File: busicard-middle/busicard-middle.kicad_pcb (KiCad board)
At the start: 2 copper layers, 70 x 46 mm, 8 parts

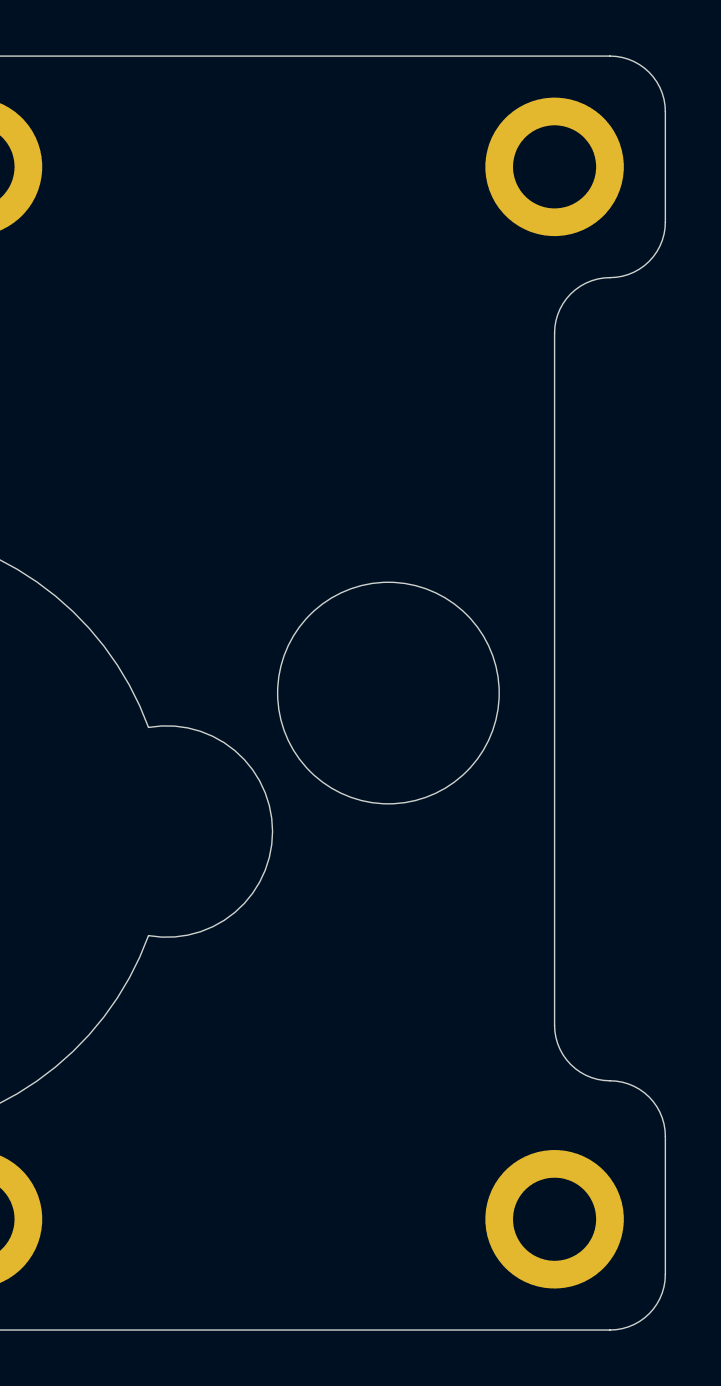
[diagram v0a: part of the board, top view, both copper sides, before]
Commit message: First pass at ready for production
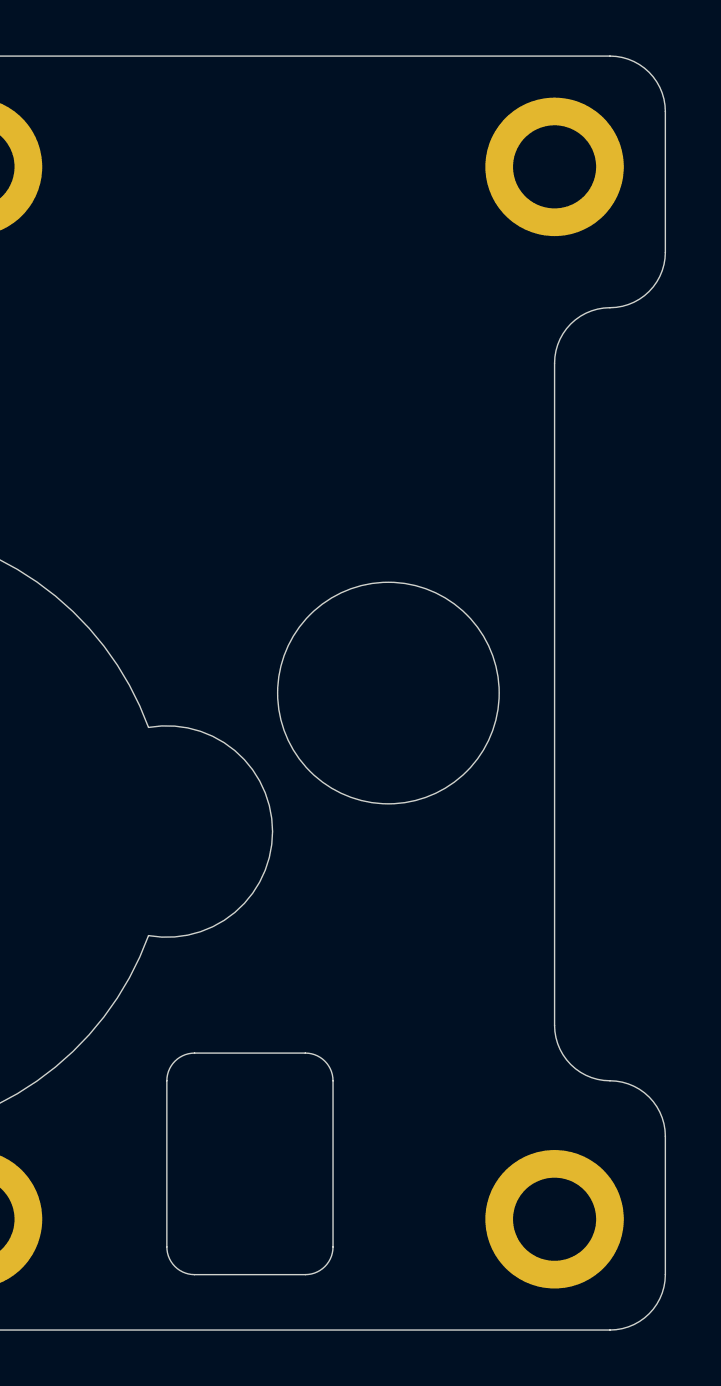
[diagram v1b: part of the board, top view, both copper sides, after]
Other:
- outline, holes or cut-outs redrawn
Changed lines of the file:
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@@
+	)
+	(gr_rect
+		(start 182 113)
+		(end 188 121)
+		(stroke
+			(width 0.1)
+			(type dot)
+		)
+		(fill none)
+		(layer "Dwgs.User")
 	)
 	(gr_rect
@@
 		(layer "Edge.Cuts")
 	)
+	(gr_line
+		(start 183 121)
+		(end 187 121)
+		(stroke
+			(width 0.05)
+			(type default)
+		)
+		(layer "Edge.Cuts")
+	)
 	(gr_arc
 		(start 155.337728 91.240826)
@@
 	)
 	(gr_arc
-		(start 196 87)
-		(mid 196.585786 85.585786)
-		(end 198 85)
+		(start 188 120)
+		(mid 187.707107 120.707107)
+		(end 187 121)
+		(stroke
+			(width 0.05)
+			(type default)
+		)
+		(layer "Edge.Cuts")
+	)
+	(gr_line
+		(start 188 120)
+		(end 188 114)
+		(stroke
+			(width 0.05)
+			(type default)
+		)
+		(layer "Edge.Cuts")
+	)
+	(gr_arc
+		(start 196 88.085786)
+		(mid 196.585786 86.671572)
+		(end 198 86.085786)
+		(stroke
+			(width 0.05)
+			(type default)
+		)
+		(layer "Edge.Cuts")
+	)
+	(gr_arc
+		(start 182 114)
+		(mid 182.292893 113.292893)
+		(end 183 113)
 		(stroke
 			(width 0.05)
@@
 		(layer "Edge.Cuts")
 	)
+	(gr_line
+		(start 183 113)
+		(end 187 113)
+		(stroke
+			(width 0.05)
+			(type default)
+		)
+		(layer "Edge.Cuts")
+	)
 	(gr_arc
 		(start 198 114)
@@
 		(layer "Edge.Cuts")
 	)
-	(gr_line
-		(start 196 87)
-		(end 196 112)
+	(gr_arc
+		(start 187 113)
+		(mid 187.707107 113.292893)
+		(end 188 114)
 		(stroke
 			(width 0.05)
@@
 	)
 	(gr_line
+		(start 200 84.085786)
+		(end 200 79)
+		(stroke
+			(width 0.05)
+			(type default)
+		)
+		(layer "Edge.Cuts")
+	)
+	(gr_line
 		(start 130 121)
 		(end 130 79)
@@
 	)
 	(gr_line
-		(start 200 79)
-		(end 200 83)
+		(start 196 88.085786)
+		(end 196 112)
 		(stroke
 			(width 0.05)
@@
 	)
 	(gr_arc
-		(start 200 83)
-		(mid 199.414214 84.414214)
-		(end 198 85)
+		(start 200 84.085786)
+		(mid 199.414214 85.5)
+		(end 198 86.085786)
+		(stroke
+			(width 0.05)
+			(type default)
+		)
+		(layer "Edge.Cuts")
+	)
+	(gr_line
+		(start 182 120)
+		(end 182 114)
 		(stroke
 			(width 0.05)
@@
 		(stroke
 			(width 0.05)
+			(type default)
+		)
+		(layer "Edge.Cuts")
+	)
+	(gr_arc
+		(start 183 121)
+		(mid 182.292893 120.707107)
+		(end 182 120)
+		(stroke
+			(width 0.05)

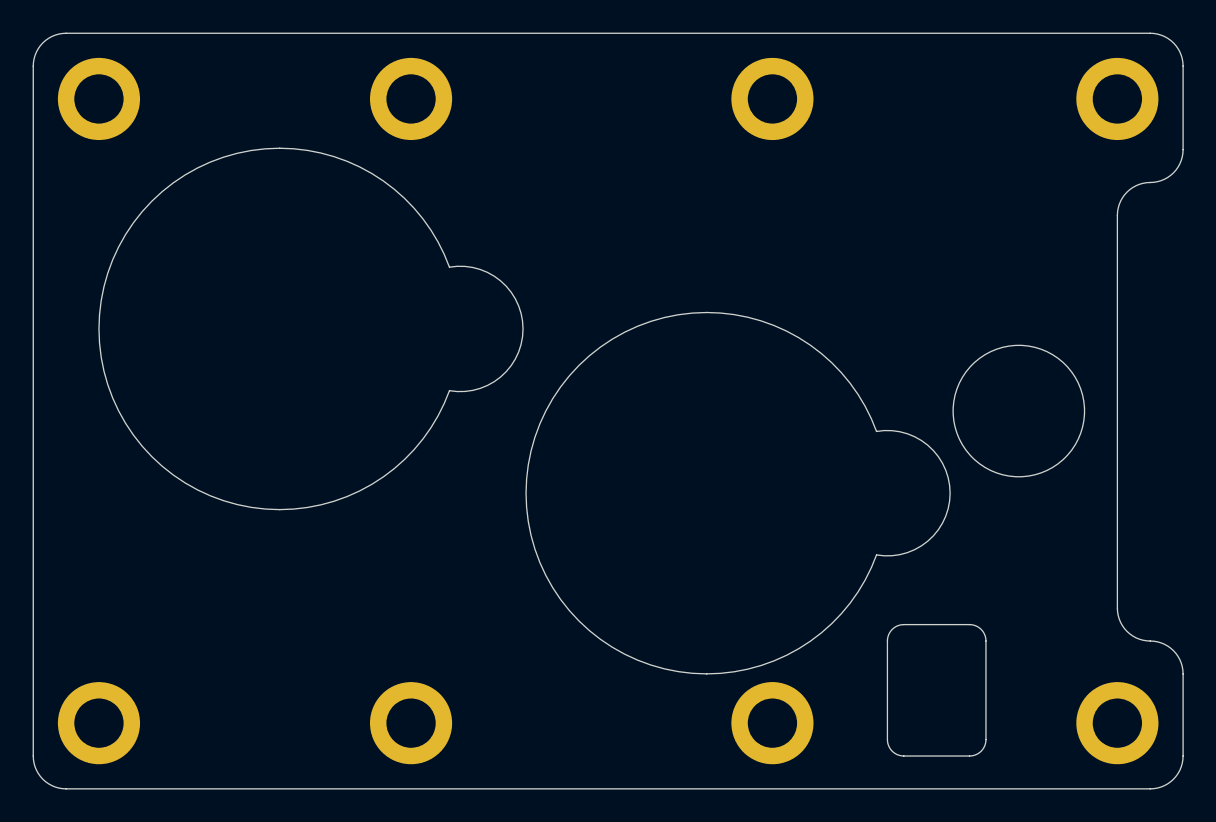
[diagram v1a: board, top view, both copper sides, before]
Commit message: More steps to production
- add slik
- add paste to battery pads
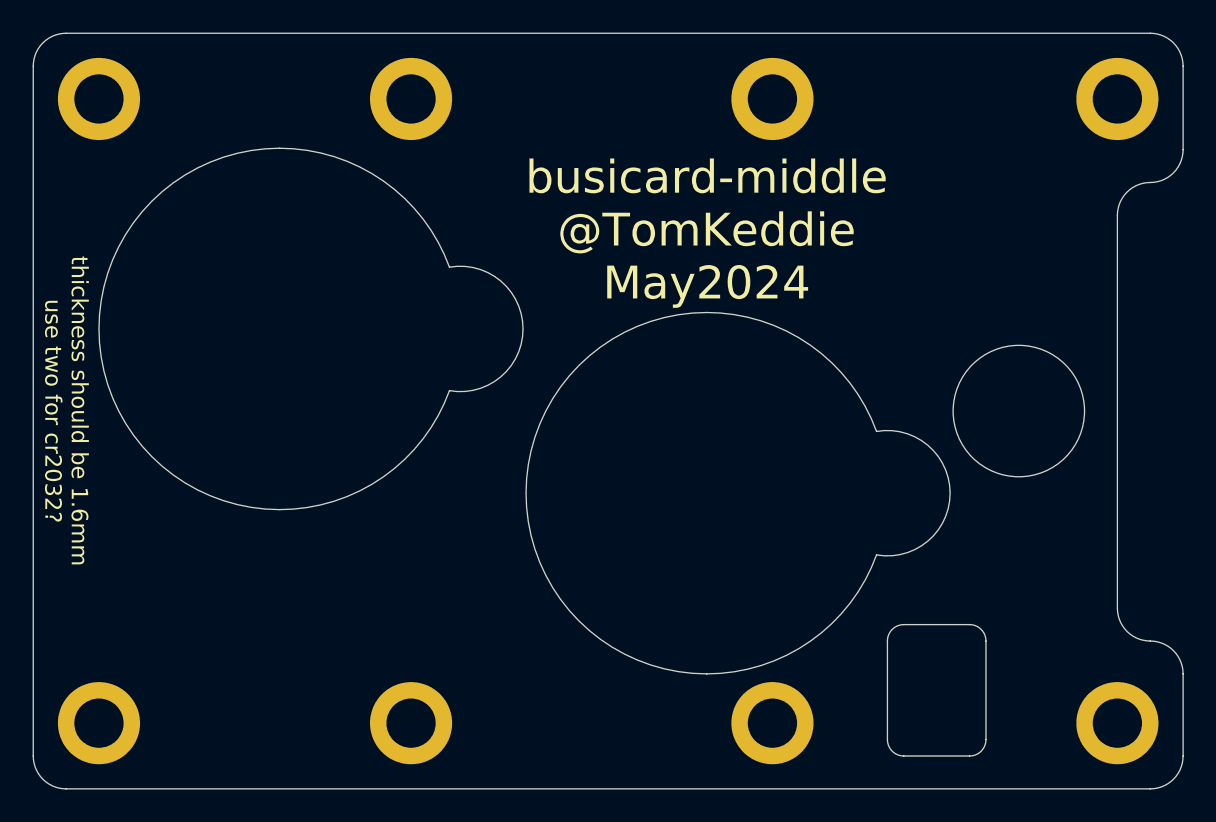
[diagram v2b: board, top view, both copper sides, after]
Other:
- board text added: "busicard-middle @TomKeddie May2024"
- board text added: "thickness should be 1.6mm use two for cr2032?"
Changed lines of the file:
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@@
 		(layer "Edge.Cuts")
 	)
+	(gr_text "thickness should be 1.6mm\nuse two for cr2032?"
+		(at 132 100 270)
+		(layer "F.SilkS")
+		(effects
+			(font
+				(size 1 1)
+				(thickness 0.1)
+			)
+		)
+	)
+	(gr_text "busicard-middle\n@TomKeddie\nMay2024"
+		(at 171 89 0)
+		(layer "F.SilkS")
+		(effects
+			(font
+				(size 2 2)
+				(thickness 0.3)
+			)
+		)
+	)
 )

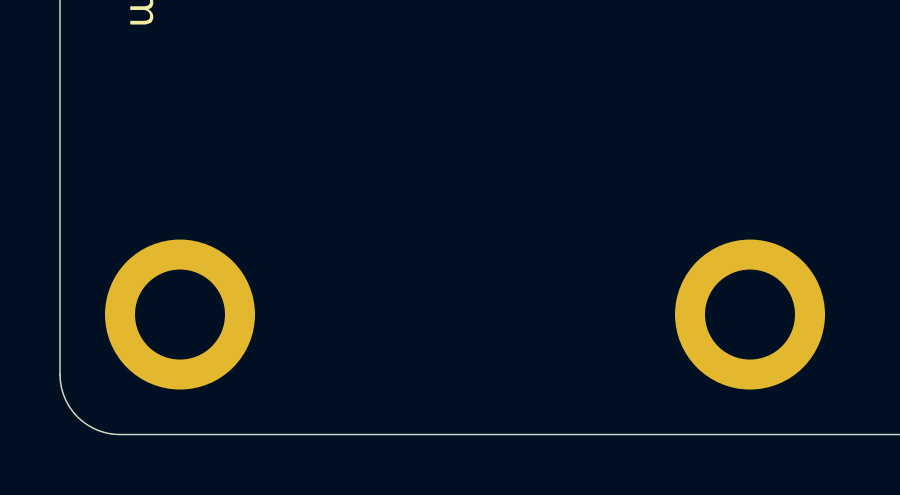
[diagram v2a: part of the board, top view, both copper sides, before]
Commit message: Add assembly holes and batch number on silkscreen
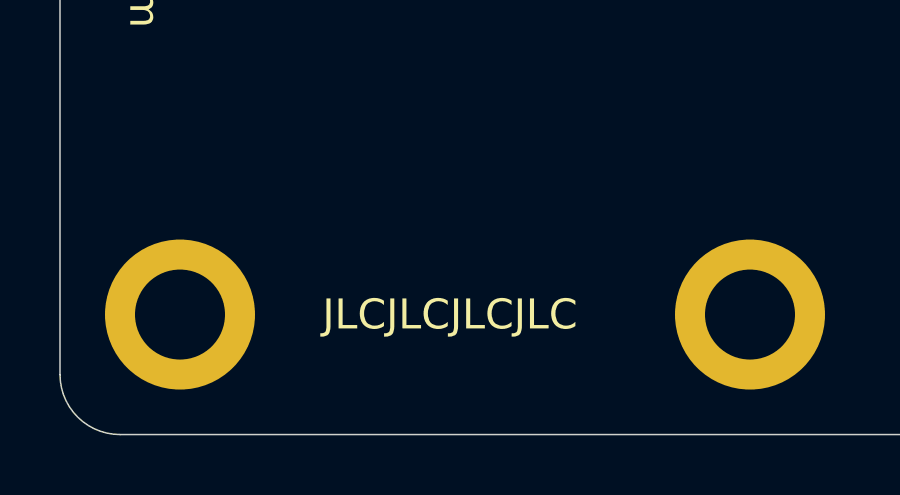
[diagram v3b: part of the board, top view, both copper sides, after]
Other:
- board text added: "JLCJLCJLCJLC"
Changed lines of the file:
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@@
 		(layer "Edge.Cuts")
+	)
+	(gr_text "JLCJLCJLCJLC"
+		(at 143 119 0)
+		(layer "F.SilkS")
+		(effects
+			(font
+				(size 1 1)
+				(thickness 0.1)
+			)
+		)
 	)
 	(gr_text "thickness should be 1.6mm\nuse two for cr2032?"

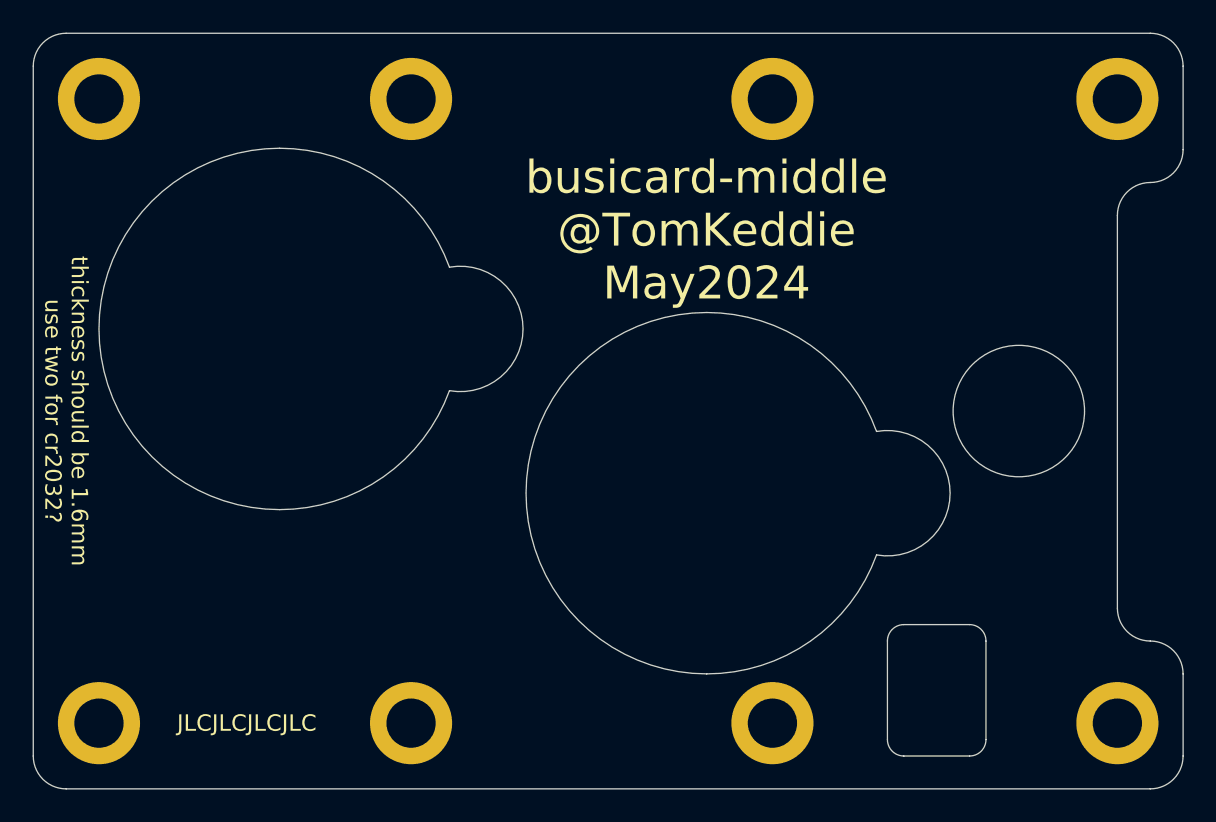
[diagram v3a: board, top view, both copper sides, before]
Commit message: busicard-top: enlarge battery opening
move all mount points 0.5mm towards edges
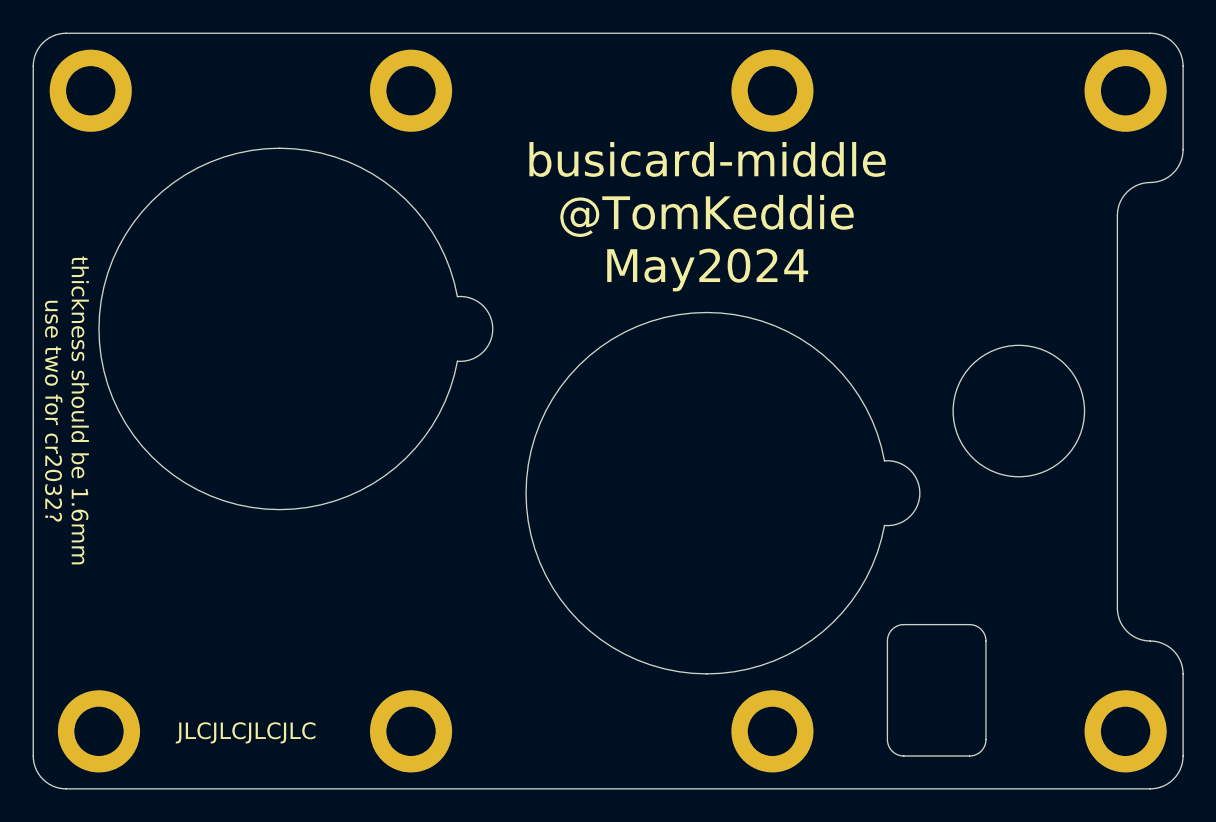
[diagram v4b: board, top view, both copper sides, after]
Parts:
- moved TP10 0.71 mm to (133.5, 80.5)
- moved TP5 0.71 mm to (196.5, 119.5)
- moved TP6 0.71 mm to (196.5, 80.5)
- moved TP1 0.50 mm to (175.0, 80.5)
- moved TP4 0.50 mm to (134.0, 119.5)
- moved TP7 0.50 mm to (153.0, 119.5)
- moved TP8 0.50 mm to (153.0, 80.5)
- moved TP9 0.50 mm to (175.0, 119.5)
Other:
- outline, holes or cut-outs redrawn
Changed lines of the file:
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@@
 	(footprint "lib:interconnect-middle"
 		(layer "F.Cu")
-		(at 175 119)
+		(at 175 119.5)
 		(property "Reference" "TP9"
 			(at 0 -2.25 0)
@@
 	(footprint "lib:interconnect-middle"
 		(layer "F.Cu")
-		(at 175 81)
+		(at 175 80.5)
 		(property "Reference" "TP1"
 			(at 0 -2.25 0)
@@
 	(footprint "lib:interconnect-middle"
 		(layer "F.Cu")
-		(at 134 81)
+		(at 133.5 80.5)
 		(property "Reference" "TP10"
 			(at 0 -2.25 0)
@@
 	(footprint "lib:interconnect-middle"
 		(layer "F.Cu")
-		(at 196 119)
+		(at 196.5 119.5)
 		(property "Reference" "TP5"
 			(at 0 -2.25 0)
@@
 	(footprint "lib:interconnect-middle"
 		(layer "F.Cu")
-		(at 196 81)
+		(at 196.5 80.5)
 		(property "Reference" "TP6"
 			(at 0 -2.25 0)
@@
 	(footprint "lib:interconnect-middle"
 		(layer "F.Cu")
-		(at 153 81)
+		(at 153 80.5)
 		(property "Reference" "TP8"
 			(at 0 -2.25 0)
@@
 	(footprint "lib:interconnect-middle"
 		(layer "F.Cu")
-		(at 134 119)
+		(at 134 119.5)
 		(property "Reference" "TP4"
 			(at 0 -2.25 0)
@@
 	(footprint "lib:interconnect-middle"
 		(layer "F.Cu")
-		(at 153 119)
+		(at 153 119.5)
 		(property "Reference" "TP7"
 			(at 0 -2.25 0)
@@
 		(layer "Edge.Cuts")
 	)
-	(gr_arc
-		(start 155.337728 91.240826)
-		(mid 159.817066 95)
-		(end 155.337728 98.759174)
-		(stroke
-			(width 0.05)
-			(type default)
-		)
-		(layer "Edge.Cuts")
-	)
 	(gr_line
 		(start 200 116)
@@
 	)
 	(gr_arc
-		(start 145 84)
-		(mid 151.310669 85.990258)
-		(end 155.337728 91.240826)
+		(start 181.822569 106.96774)
+		(mid 178.048222 113.445269)
+		(end 171 116)
 		(stroke
 			(width 0.05)
@@
 		(layer "Edge.Cuts")
 	)
-	(gr_arc
-		(start 181.337728 108.759174)
-		(mid 177.310669 114.009743)
-		(end 171 116)
-		(stroke
-			(width 0.05)
-			(type default)
-		)
-		(layer "Edge.Cuts")
-	)
-	(gr_arc
-		(start 155.337728 98.759174)
-		(mid 151.310669 104.009743)
-		(end 145 106)
-		(stroke
-			(width 0.05)
-			(type default)
-		)
-		(layer "Edge.Cuts")
-	)
 	(gr_line
 		(start 183 113)
@@
 	)
 	(gr_arc
-		(start 171 94)
-		(mid 177.310669 95.990258)
-		(end 181.337728 101.240826)
-		(stroke
-			(width 0.05)
-			(type default)
-		)
-		(layer "Edge.Cuts")
-	)
-	(gr_arc
 		(start 200 121)
 		(mid 199.414214 122.414214)
@@
 	)
 	(gr_arc
+		(start 155.822569 93.03226)
+		(mid 157.975723 95)
+		(end 155.822569 96.96774)
+		(stroke
+			(width 0.05)
+			(type default)
+		)
+		(layer "Edge.Cuts")
+	)
+	(gr_arc
 		(start 187 113)
 		(mid 187.707107 113.292893)
@@
 	)
 	(gr_arc
-		(start 181.337728 101.240826)
-		(mid 185.817066 105)
-		(end 181.337728 108.759174)
+		(start 145 84)
+		(mid 152.048222 86.554731)
+		(end 155.822569 93.03226)
+		(stroke
+			(width 0.05)
+			(type default)
+		)
+		(layer "Edge.Cuts")
+	)
+	(gr_arc
+		(start 171 94)
+		(mid 178.048222 96.554731)
+		(end 181.822569 103.03226)
 		(stroke
 			(width 0.05)
@@
 		(layer "Edge.Cuts")
 	)
+	(gr_arc
+		(start 155.822569 96.96774)
+		(mid 152.048222 103.445269)
+		(end 145 106)
+		(stroke
+			(width 0.05)
+			(type default)
+		)
+		(layer "Edge.Cuts")
+	)
 	(gr_line
 		(start 198 123)
@@
 	)
 	(gr_arc
+		(start 181.822569 103.03226)
+		(mid 183.975723 105)
+		(end 181.822569 106.96774)
+		(stroke
+			(width 0.05)
+			(type default)
+		)
+		(layer "Edge.Cuts")
+	)
+	(gr_arc
 		(start 183 121)
 		(mid 182.292893 120.707107)
@@
 	)
 	(gr_text "JLCJLCJLCJLC"
-		(at 143 119 0)
+		(at 143 119.5 0)
 		(layer "F.SilkS")
 		(effects
@@
 	)
 	(gr_text "busicard-middle\n@TomKeddie\nMay2024"
-		(at 171 89 0)
+		(at 171 88 0)
 		(layer "F.SilkS")
 		(effects
